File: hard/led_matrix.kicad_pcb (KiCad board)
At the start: 2 copper layers, 150 x 150 mm, 1038 parts, among them J1 MicroXNJ

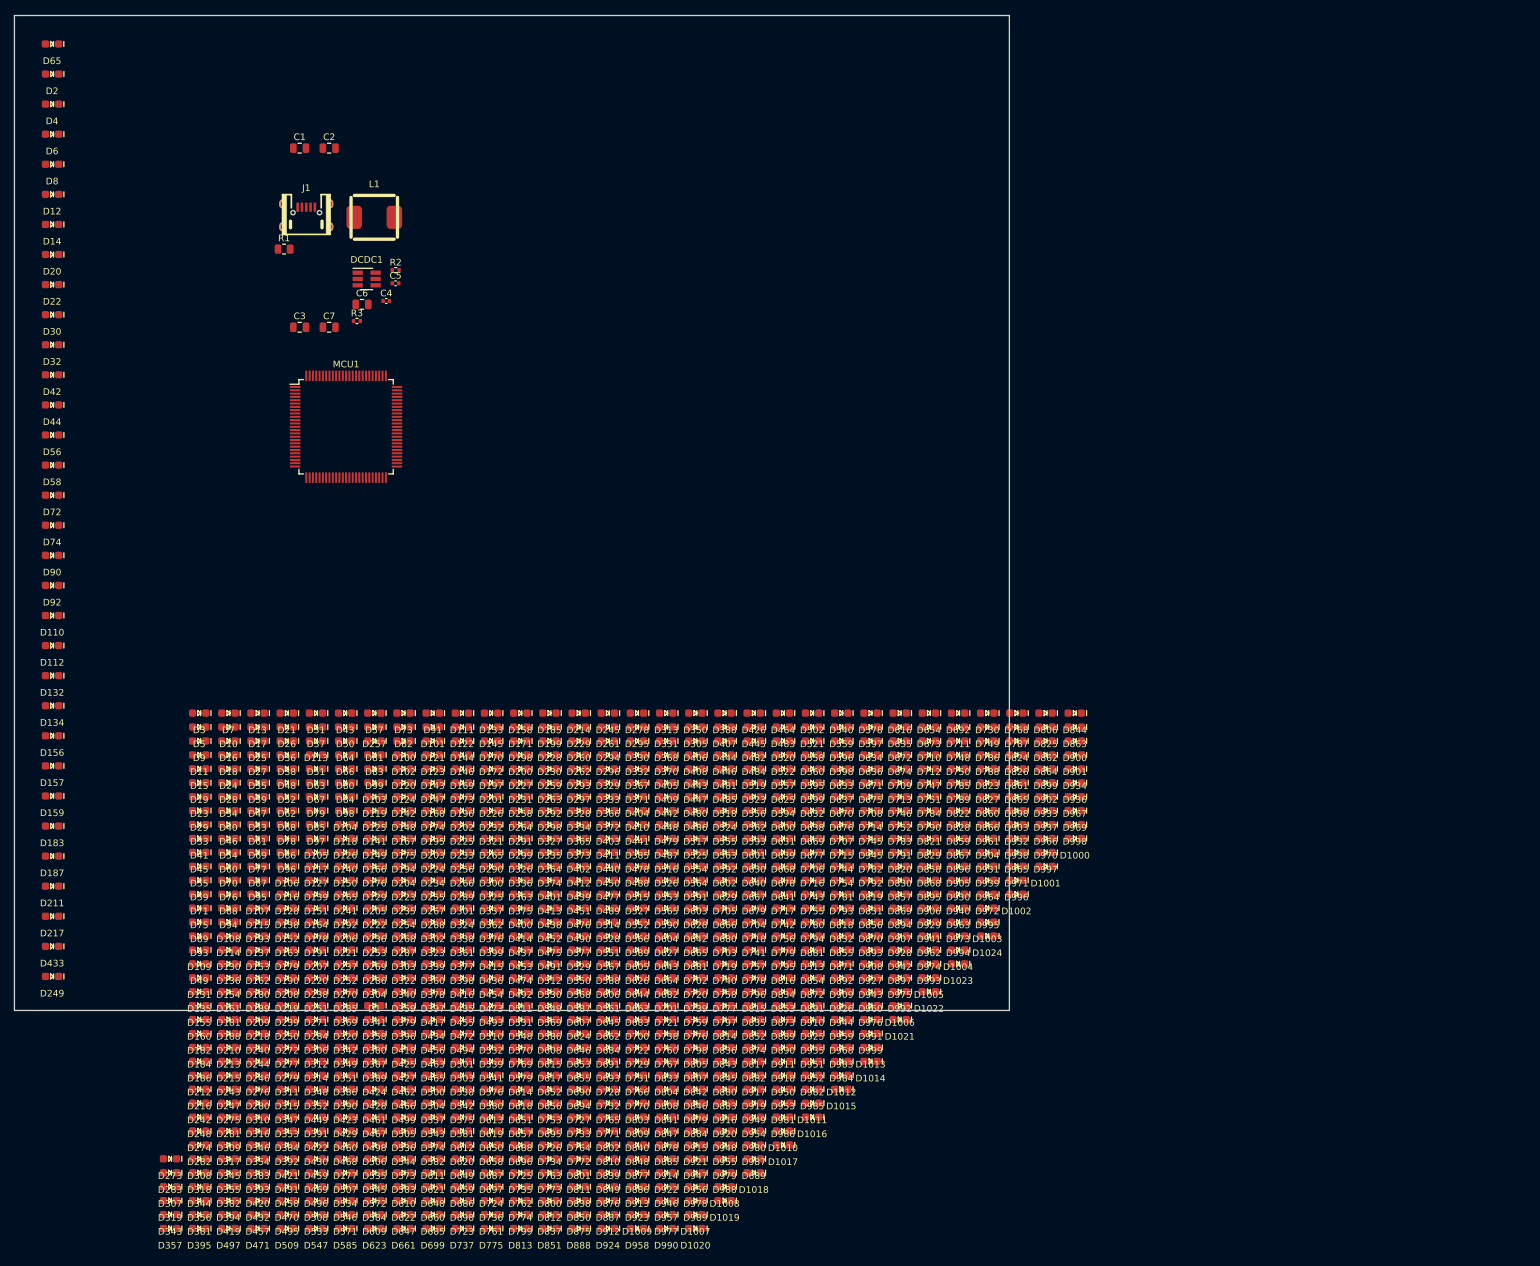
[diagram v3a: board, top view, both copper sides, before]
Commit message: 32x32 leds on board
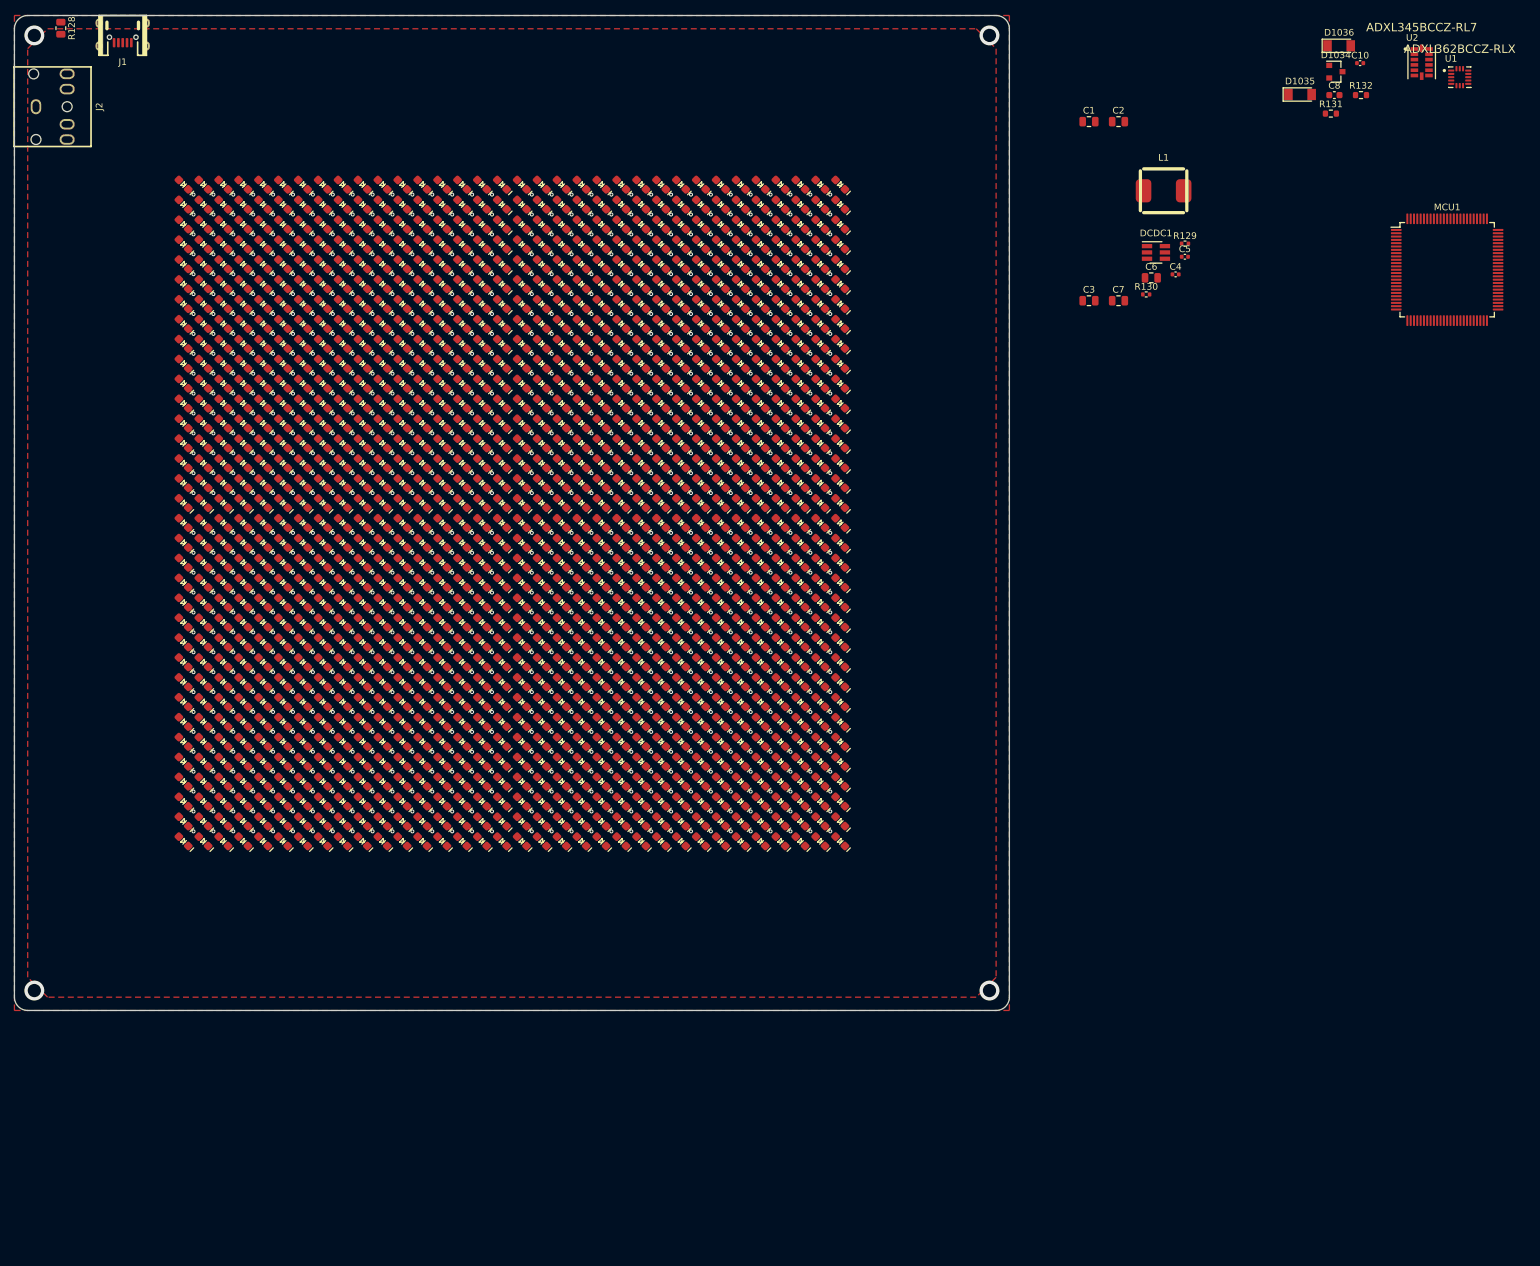
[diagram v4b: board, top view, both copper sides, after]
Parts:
- removed the D1 at (74.3, 177.2)
- removed D10, D100, D1000, D1001, D1002, D1003, D1004, D1005, D1006, D1007, D1008, D1009, D101, D1010, D1011, D1012, D1013, D1014, D1015, D1016, D1017, D1018, D1019, D102, D1020, D1021, D1022, D1023, D1024, D103, D104, D105, D106, D107, D108, D109, D11, D110, D111, D112, D113, D114, D115, D116, D117, D118, D119, D12, D120, D121, D122, D123, D124, D125, D126, D127, D128, D129, D13, D130, D131, D132, D133, D134, D135, D136, D137, D138, D139, D14, D140, D141, D142, D143, D144, D145, D146, D147, D148, D149, D15, D150, D151, D152, D153, D154, D155, D156, D157, D158, D159, D16, D160, D161, D162, D163, D164, D165, D166, D167, D168, D169, D17, D170, D171, D172, D173, D174, D175, D176, D177, D178, D179, D18, D180, D181, D182, D183, D184, D185, D186, D187, D188, D189, D19, D190, D191, D192, D193, D194, D195, D196, D197, D198, D199, D20, D200, D201, D202, D203, D204, D205, D206, D207, D208, D209, D21, D210, D211, D212, D213, D214, D215, D216, D217, D218, D219, D22, D220, D221, D222, D223, D224, D225, D226, D227, D228, D229, D23, D230, D231, D232, D233, D234, D235, D236, D237, D238, D239, D24, D240, D241, D242, D243, D244, D245, D246, D247, D248, D249, D25, D250, D251, D252, D253, D254, D255, D256, D257, D258, D259, D26, D260, D261, D262, D263, D264, D265, D266, D267, D268, D269, D27, D270, D271, D272, D273, D274, D275, D276, D277, D278, D279, D28, D280, D281, D282, D283, D284, D285, D286, D287, D288, D289, D29, D290, D291, D292, D293, D294, D295, D296, D297, D298, D299, D30, D300, D301, D302, D303, D304, D305, D306, D307, D308, D309, D31, D310, D311, D312, D313, D314, D315, D316, D317, D318, D319, D32, D320, D321, D322, D323, D324, D325, D326, D327, D328, D329, D330, D331, D332, D333, D334, D335, D336, D337, D338, D339, D340, D341, D342, D343, D344, D345, D346, D347, D348, D349, D350, D351, D352, D353, D354, D355, D356, D357, D358, D359, D36, D360, D361, D362, D363, D364, D365, D366, D367, D368, D369, D37, D370, D371, D372, D373, D374, D375, D376, D377, D378, D379, D38, D380, D381, D382, D383, D384, D385, D386, D387, D388, D389, D39, D390, D391, D392, D393, D394, D395, D396, D397, D398, D399, D4, D40, D400, D401, D402, D403, D404, D405, D406, D407, D408, D409, D41, D410, D411, D412, D413, D414, D415, D416, D417, D418, D419, D42, D420, D421, D422, D423, D424, D425, D426, D427, D428, D429, D43, D430, D431, D432, D433, D434, D435, D436, D437, D438, D439, D44, D440, D441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: LTST-S270TBKT, led_matrix:LED_LiteOn_LTST-S270TBKT
- removed the D2 at (25.7, 38.8)
- removed the D3 at (47.9, 135.2)
- removed the D33 at (47.9, 152.0)
- removed the D34 at (52.3, 147.8)
- removed the D35 at (56.7, 143.6)
- removed the D65 at (25.7, 34.3)
- removed the D66 at (69.9, 141.5)
- removed the D67 at (65.5, 145.7)
- removed R1: 0R1, Resistor_SMD:R_0805_2012Metric
- added C10: 0u1/6V3, Capacitor_SMD:C_0402_1005Metric, F.Cu at (222.9, 37.2)
- added C8: 1u/6V3, Capacitor_SMD:C_0603_1608Metric, F.Cu at (219.0, 42.0)
- added D1: LTST-S270TBKT, led_matrix:LED_LiteOn_LTST-S270TBKT, F.Cu at (54.5, 124.5)
- added D1: LTST-S270TBKT, led_matrix:LED_LiteOn_LTST-S270TBKT, F.Cu at (45.5, 151.5)
- added D1: LTST-S270TBKT, led_matrix:LED_LiteOn_LTST-S270TBKT, F.Cu at (132.5, 73.5)
- added D1: LTST-S270TBKT, led_matrix:LED_LiteOn_LTST-S270TBKT, F.Cu at (132.5, 55.5)
- added D1: LTST-S270TBKT, led_matrix:LED_LiteOn_LTST-S270TBKT, F.Cu at (141.5, 82.5)
- added D1: LTST-S270TBKT, led_matrix:LED_LiteOn_LTST-S270TBKT, F.Cu at (54.5, 91.5)
- added D1: LTST-S270TBKT, led_matrix:LED_LiteOn_LTST-S270TBKT, F.Cu at (45.5, 91.5)
- added D1: LTST-S270TBKT, led_matrix:LED_LiteOn_LTST-S270TBKT, F.Cu at (81.5, 91.5)
- added D1: LTST-S270TBKT, led_matrix:LED_LiteOn_LTST-S270TBKT, F.Cu at (45.5, 100.5)
- added D1: LTST-S270TBKT, led_matrix:LED_LiteOn_LTST-S270TBKT, F.Cu at (54.5, 100.5)
- added D1: LTST-S270TBKT, led_matrix:LED_LiteOn_LTST-S270TBKT, F.Cu at (45.5, 55.5)
- added D1: LTST-S270TBKT, led_matrix:LED_LiteOn_LTST-S270TBKT, F.Cu at (81.5, 55.5)
- added D1: LTST-S270TBKT, led_matrix:LED_LiteOn_LTST-S270TBKT, F.Cu at (54.5, 151.5)
- added D1: LTST-S270TBKT, led_matrix:LED_LiteOn_LTST-S270TBKT, F.Cu at (81.5, 73.5)
- added D1: LTST-S270TBKT, led_matrix:LED_LiteOn_LTST-S270TBKT, F.Cu at (81.5, 82.5)
- added D1: LTST-S270TBKT, led_matrix:LED_LiteOn_LTST-S270TBKT, F.Cu at (90.5, 82.5)
- added D1: LTST-S270TBKT, led_matrix:LED_LiteOn_LTST-S270TBKT, F.Cu at (90.5, 73.5)
- added D1: LTST-S270TBKT, led_matrix:LED_LiteOn_LTST-S270TBKT, F.Cu at (96.5, 106.5)
- added D1: LTST-S270TBKT, led_matrix:LED_LiteOn_LTST-S270TBKT, F.Cu at (105.5, 151.5)
- added D1: LTST-S270TBKT, led_matrix:LED_LiteOn_LTST-S270TBKT, F.Cu at (132.5, 133.5)
- added D1: LTST-S270TBKT, led_matrix:LED_LiteOn_LTST-S270TBKT, F.Cu at (132.5, 124.5)
- added D1: LTST-S270TBKT, led_matrix:LED_LiteOn_LTST-S270TBKT, F.Cu at (132.5, 106.5)
- added D1: LTST-S270TBKT, led_matrix:LED_LiteOn_LTST-S270TBKT, F.Cu at (141.5, 133.5)
- added D1: LTST-S270TBKT, led_matrix:LED_LiteOn_LTST-S270TBKT, F.Cu at (81.5, 142.5)
- added D1: LTST-S270TBKT, led_matrix:LED_LiteOn_LTST-S270TBKT, F.Cu at (54.5, 142.5)
- added D1: LTST-S270TBKT, led_matrix:LED_LiteOn_LTST-S270TBKT, F.Cu at (123.5, 142.5)
- added D1: LTST-S270TBKT, led_matrix:LED_LiteOn_LTST-S270TBKT, F.Cu at (132.5, 151.5)
- added D1: LTST-S270TBKT, led_matrix:LED_LiteOn_LTST-S270TBKT, F.Cu at (105.5, 115.5)
- added D1: LTST-S270TBKT, led_matrix:LED_LiteOn_LTST-S270TBKT, F.Cu at (96.5, 115.5)
- added D1: LTST-S270TBKT, led_matrix:LED_LiteOn_LTST-S270TBKT, F.Cu at (132.5, 142.5)
- added D1: LTST-S270TBKT, led_matrix:LED_LiteOn_LTST-S270TBKT, F.Cu at (96.5, 142.5)
- added D1: LTST-S270TBKT, led_matrix:LED_LiteOn_LTST-S270TBKT, F.Cu at (105.5, 142.5)
- added D1: LTST-S270TBKT, led_matrix:LED_LiteOn_LTST-S270TBKT, F.Cu at (105.5, 106.5)
- added D1: LTST-S270TBKT, led_matrix:LED_LiteOn_LTST-S270TBKT, F.Cu at (96.5, 151.5)
- added D1: LTST-S270TBKT, led_matrix:LED_LiteOn_LTST-S270TBKT, F.Cu at (81.5, 106.5)
- added D1: LTST-S270TBKT, led_matrix:LED_LiteOn_LTST-S270TBKT, F.Cu at (45.5, 73.5)
- added D1: LTST-S270TBKT, led_matrix:LED_LiteOn_LTST-S270TBKT, F.Cu at (63.5, 82.5)
- added D1: LTST-S270TBKT, led_matrix:LED_LiteOn_LTST-S270TBKT, F.Cu at (72.5, 82.5)
- added D1: LTST-S270TBKT, led_matrix:LED_LiteOn_LTST-S270TBKT, F.Cu at (45.5, 82.5)
- added D1: LTST-S270TBKT, led_matrix:LED_LiteOn_LTST-S270TBKT, F.Cu at (54.5, 82.5)
- added D1: LTST-S270TBKT, led_matrix:LED_LiteOn_LTST-S270TBKT, F.Cu at (54.5, 73.5)
- added D1: LTST-S270TBKT, led_matrix:LED_LiteOn_LTST-S270TBKT, F.Cu at (72.5, 73.5)
- added D1: LTST-S270TBKT, led_matrix:LED_LiteOn_LTST-S270TBKT, F.Cu at (63.5, 73.5)
- added D1: LTST-S270TBKT, led_matrix:LED_LiteOn_LTST-S270TBKT, F.Cu at (90.5, 55.5)
- added D1: LTST-S270TBKT, led_matrix:LED_LiteOn_LTST-S270TBKT, F.Cu at (90.5, 64.5)
- added D1: LTST-S270TBKT, led_matrix:LED_LiteOn_LTST-S270TBKT, F.Cu at (81.5, 124.5)
- added D1: LTST-S270TBKT, led_matrix:LED_LiteOn_LTST-S270TBKT, F.Cu at (81.5, 64.5)
- added D1: LTST-S270TBKT, led_matrix:LED_LiteOn_LTST-S270TBKT, F.Cu at (63.5, 64.5)
- added D1: LTST-S270TBKT, led_matrix:LED_LiteOn_LTST-S270TBKT, F.Cu at (72.5, 64.5)
- added D1: LTST-S270TBKT, led_matrix:LED_LiteOn_LTST-S270TBKT, F.Cu at (72.5, 55.5)
- added D1: LTST-S270TBKT, led_matrix:LED_LiteOn_LTST-S270TBKT, F.Cu at (63.5, 55.5)
- added D1: LTST-S270TBKT, led_matrix:LED_LiteOn_LTST-S270TBKT, F.Cu at (81.5, 133.5)
- added D1: LTST-S270TBKT, led_matrix:LED_LiteOn_LTST-S270TBKT, F.Cu at (90.5, 133.5)
- added D1: LTST-S270TBKT, led_matrix:LED_LiteOn_LTST-S270TBKT, F.Cu at (63.5, 133.5)
- added D1: LTST-S270TBKT, led_matrix:LED_LiteOn_LTST-S270TBKT, F.Cu at (90.5, 124.5)
- added D1: LTST-S270TBKT, led_matrix:LED_LiteOn_LTST-S270TBKT, F.Cu at (45.5, 124.5)
- added D1: LTST-S270TBKT, led_matrix:LED_LiteOn_LTST-S270TBKT, F.Cu at (54.5, 133.5)
- added D1: LTST-S270TBKT, led_matrix:LED_LiteOn_LTST-S270TBKT, F.Cu at (90.5, 91.5)
- added D1: LTST-S270TBKT, led_matrix:LED_LiteOn_LTST-S270TBKT, F.Cu at (90.5, 100.5)
- added D1: LTST-S270TBKT, led_matrix:LED_LiteOn_LTST-S270TBKT, F.Cu at (63.5, 100.5)
- added D1: LTST-S270TBKT, led_matrix:LED_LiteOn_LTST-S270TBKT, F.Cu at (72.5, 100.5)
- added D1: LTST-S270TBKT, led_matrix:LED_LiteOn_LTST-S270TBKT, F.Cu at (81.5, 100.5)
- added D1: LTST-S270TBKT, led_matrix:LED_LiteOn_LTST-S270TBKT, F.Cu at (72.5, 91.5)
- added D1: LTST-S270TBKT, led_matrix:LED_LiteOn_LTST-S270TBKT, F.Cu at (63.5, 91.5)
- added D1: LTST-S270TBKT, led_matrix:LED_LiteOn_LTST-S270TBKT, F.Cu at (45.5, 64.5)
- added D1: LTST-S270TBKT, led_matrix:LED_LiteOn_LTST-S270TBKT, F.Cu at (54.5, 64.5)
- added D1: LTST-S270TBKT, led_matrix:LED_LiteOn_LTST-S270TBKT, F.Cu at (90.5, 142.5)
- added D1: LTST-S270TBKT, led_matrix:LED_LiteOn_LTST-S270TBKT, F.Cu at (72.5, 133.5)
- added D1: LTST-S270TBKT, led_matrix:LED_LiteOn_LTST-S270TBKT, F.Cu at (63.5, 151.5)
- added D1: LTST-S270TBKT, led_matrix:LED_LiteOn_LTST-S270TBKT, F.Cu at (90.5, 151.5)
- added D1: LTST-S270TBKT, led_matrix:LED_LiteOn_LTST-S270TBKT, F.Cu at (72.5, 151.5)
- added D1: LTST-S270TBKT, led_matrix:LED_LiteOn_LTST-S270TBKT, F.Cu at (81.5, 151.5)
- added D1: LTST-S270TBKT, led_matrix:LED_LiteOn_LTST-S270TBKT, F.Cu at (72.5, 142.5)
- added D1: LTST-S270TBKT, led_matrix:LED_LiteOn_LTST-S270TBKT, F.Cu at (63.5, 142.5)
- added D1: LTST-S270TBKT, led_matrix:LED_LiteOn_LTST-S270TBKT, F.Cu at (45.5, 115.5)
- added D1: LTST-S270TBKT, led_matrix:LED_LiteOn_LTST-S270TBKT, F.Cu at (54.5, 115.5)
- added D1: LTST-S270TBKT, led_matrix:LED_LiteOn_LTST-S270TBKT, F.Cu at (54.5, 106.5)
- added D1: LTST-S270TBKT, led_matrix:LED_LiteOn_LTST-S270TBKT, F.Cu at (123.5, 133.5)
- added D1: LTST-S270TBKT, led_matrix:LED_LiteOn_LTST-S270TBKT, F.Cu at (45.5, 133.5)
- added D1: LTST-S270TBKT, led_matrix:LED_LiteOn_LTST-S270TBKT, F.Cu at (105.5, 133.5)
- added D1: LTST-S270TBKT, led_matrix:LED_LiteOn_LTST-S270TBKT, F.Cu at (54.5, 55.5)
- added D1: LTST-S270TBKT, led_matrix:LED_LiteOn_LTST-S270TBKT, F.Cu at (123.5, 82.5)
- added D1: LTST-S270TBKT, led_matrix:LED_LiteOn_LTST-S270TBKT, F.Cu at (105.5, 82.5)
- added D1: LTST-S270TBKT, led_matrix:LED_LiteOn_LTST-S270TBKT, F.Cu at (114.5, 82.5)
- added D1: LTST-S270TBKT, led_matrix:LED_LiteOn_LTST-S270TBKT, F.Cu at (96.5, 82.5)
- added D1: LTST-S270TBKT, led_matrix:LED_LiteOn_LTST-S270TBKT, F.Cu at (96.5, 73.5)
- added D1: LTST-S270TBKT, led_matrix:LED_LiteOn_LTST-S270TBKT, F.Cu at (141.5, 73.5)
- added D1: LTST-S270TBKT, led_matrix:LED_LiteOn_LTST-S270TBKT, F.Cu at (105.5, 73.5)
- added D1: LTST-S270TBKT, led_matrix:LED_LiteOn_LTST-S270TBKT, F.Cu at (123.5, 73.5)
- added D1: LTST-S270TBKT, led_matrix:LED_LiteOn_LTST-S270TBKT, F.Cu at (72.5, 124.5)
- added D1: LTST-S270TBKT, led_matrix:LED_LiteOn_LTST-S270TBKT, F.Cu at (141.5, 64.5)
- added D1: LTST-S270TBKT, led_matrix:LED_LiteOn_LTST-S270TBKT, F.Cu at (141.5, 55.5)
- added D1: LTST-S270TBKT, led_matrix:LED_LiteOn_LTST-S270TBKT, F.Cu at (114.5, 73.5)
- added D1: LTST-S270TBKT, led_matrix:LED_LiteOn_LTST-S270TBKT, F.Cu at (132.5, 64.5)
- added D1: LTST-S270TBKT, led_matrix:LED_LiteOn_LTST-S270TBKT, F.Cu at (123.5, 64.5)
- added D1: LTST-S270TBKT, led_matrix:LED_LiteOn_LTST-S270TBKT, F.Cu at (114.5, 64.5)
- added D1: LTST-S270TBKT, led_matrix:LED_LiteOn_LTST-S270TBKT, F.Cu at (123.5, 55.5)
- added D1: LTST-S270TBKT, led_matrix:LED_LiteOn_LTST-S270TBKT, F.Cu at (114.5, 55.5)
- added D1: LTST-S270TBKT, led_matrix:LED_LiteOn_LTST-S270TBKT, F.Cu at (72.5, 115.5)
- added D1: LTST-S270TBKT, led_matrix:LED_LiteOn_LTST-S270TBKT, F.Cu at (90.5, 115.5)
- added D1: LTST-S270TBKT, led_matrix:LED_LiteOn_LTST-S270TBKT, F.Cu at (63.5, 124.5)
- added D1: LTST-S270TBKT, led_matrix:LED_LiteOn_LTST-S270TBKT, F.Cu at (63.5, 115.5)
- added D1: LTST-S270TBKT, led_matrix:LED_LiteOn_LTST-S270TBKT, F.Cu at (72.5, 106.5)
- added D1: LTST-S270TBKT, led_matrix:LED_LiteOn_LTST-S270TBKT, F.Cu at (81.5, 115.5)
- added D1: LTST-S270TBKT, led_matrix:LED_LiteOn_LTST-S270TBKT, F.Cu at (63.5, 106.5)
- added D1: LTST-S270TBKT, led_matrix:LED_LiteOn_LTST-S270TBKT, F.Cu at (114.5, 133.5)
- added D1: LTST-S270TBKT, led_matrix:LED_LiteOn_LTST-S270TBKT, F.Cu at (141.5, 124.5)
- added D1: LTST-S270TBKT, led_matrix:LED_LiteOn_LTST-S270TBKT, F.Cu at (96.5, 133.5)
- added D1: LTST-S270TBKT, led_matrix:LED_LiteOn_LTST-S270TBKT, F.Cu at (96.5, 124.5)
- added D1: LTST-S270TBKT, led_matrix:LED_LiteOn_LTST-S270TBKT, F.Cu at (123.5, 124.5)
- added D1: LTST-S270TBKT, led_matrix:LED_LiteOn_LTST-S270TBKT, F.Cu at (105.5, 124.5)
- added D1: LTST-S270TBKT, led_matrix:LED_LiteOn_LTST-S270TBKT, F.Cu at (90.5, 106.5)
- added D1: LTST-S270TBKT, led_matrix:LED_LiteOn_LTST-S270TBKT, F.Cu at (141.5, 115.5)
- added D1: LTST-S270TBKT, led_matrix:LED_LiteOn_LTST-S270TBKT, F.Cu at (123.5, 115.5)
- added D1: LTST-S270TBKT, led_matrix:LED_LiteOn_LTST-S270TBKT, F.Cu at (114.5, 106.5)
- added D1: LTST-S270TBKT, led_matrix:LED_LiteOn_LTST-S270TBKT, F.Cu at (114.5, 124.5)
- added D1: LTST-S270TBKT, led_matrix:LED_LiteOn_LTST-S270TBKT, F.Cu at (141.5, 106.5)
- added D1: LTST-S270TBKT, led_matrix:LED_LiteOn_LTST-S270TBKT, F.Cu at (132.5, 115.5)
- added D1: LTST-S270TBKT, led_matrix:LED_LiteOn_LTST-S270TBKT, F.Cu at (114.5, 115.5)
- added D1: LTST-S270TBKT, led_matrix:LED_LiteOn_LTST-S270TBKT, F.Cu at (123.5, 106.5)
- added D1: LTST-S270TBKT, led_matrix:LED_LiteOn_LTST-S270TBKT, F.Cu at (141.5, 142.5)
- added D1: LTST-S270TBKT, led_matrix:LED_LiteOn_LTST-S270TBKT, F.Cu at (123.5, 151.5)
- added D1: LTST-S270TBKT, led_matrix:LED_LiteOn_LTST-S270TBKT, F.Cu at (45.5, 142.5)
- added D1: LTST-S270TBKT, led_matrix:LED_LiteOn_LTST-S270TBKT, F.Cu at (141.5, 151.5)
- added D1: LTST-S270TBKT, led_matrix:LED_LiteOn_LTST-S270TBKT, F.Cu at (114.5, 142.5)
- added D1: LTST-S270TBKT, led_matrix:LED_LiteOn_LTST-S270TBKT, F.Cu at (114.5, 151.5)
- added D1: LTST-S270TBKT, led_matrix:LED_LiteOn_LTST-S270TBKT, F.Cu at (114.5, 100.5)
- added D1: LTST-S270TBKT, led_matrix:LED_LiteOn_LTST-S270TBKT, F.Cu at (141.5, 100.5)
- added D1: LTST-S270TBKT, led_matrix:LED_LiteOn_LTST-S270TBKT, F.Cu at (114.5, 91.5)
- added D1: LTST-S270TBKT, led_matrix:LED_LiteOn_LTST-S270TBKT, F.Cu at (141.5, 91.5)
- added D1: LTST-S270TBKT, led_matrix:LED_LiteOn_LTST-S270TBKT, F.Cu at (123.5, 100.5)
- added D1: LTST-S270TBKT, led_matrix:LED_LiteOn_LTST-S270TBKT, F.Cu at (123.5, 91.5)
- added D1: LTST-S270TBKT, led_matrix:LED_LiteOn_LTST-S270TBKT, F.Cu at (132.5, 100.5)
- added D1: LTST-S270TBKT, led_matrix:LED_LiteOn_LTST-S270TBKT, F.Cu at (45.5, 106.5)
- added D1: LTST-S270TBKT, led_matrix:LED_LiteOn_LTST-S270TBKT, F.Cu at (96.5, 64.5)
- added D1: LTST-S270TBKT, led_matrix:LED_LiteOn_LTST-S270TBKT, F.Cu at (105.5, 64.5)
- added D1: LTST-S270TBKT, led_matrix:LED_LiteOn_LTST-S270TBKT, F.Cu at (132.5, 91.5)
- added D1: LTST-S270TBKT, led_matrix:LED_LiteOn_LTST-S270TBKT, F.Cu at (105.5, 91.5)
- added D1: LTST-S270TBKT, led_matrix:LED_LiteOn_LTST-S270TBKT, F.Cu at (96.5, 91.5)
- added D1: LTST-S270TBKT, led_matrix:LED_LiteOn_LTST-S270TBKT, F.Cu at (96.5, 100.5)
- added D1: LTST-S270TBKT, led_matrix:LED_LiteOn_LTST-S270TBKT, F.Cu at (105.5, 55.5)
- added D1: LTST-S270TBKT, led_matrix:LED_LiteOn_LTST-S270TBKT, F.Cu at (105.5, 100.5)
- added D1: LTST-S270TBKT, led_matrix:LED_LiteOn_LTST-S270TBKT, F.Cu at (96.5, 55.5)
- added D1: LTST-S270TBKT, led_matrix:LED_LiteOn_LTST-S270TBKT, F.Cu at (132.5, 82.5)
- added D1034: PSM712-LF-T7, Package_TO_SOT_SMD:SOT-23, F.Cu at (219.2, 38.5)
- added D1035: D_Zener, Diode_SMD:D_MiniMELF, F.Cu at (213.8, 41.9)
- added D1036: D_Zener, Diode_SMD:D_MiniMELF, F.Cu at (219.7, 34.6)
- added D2: LTST-S270TBKT, led_matrix:LED_LiteOn_LTST-S270TBKT, F.Cu at (54.5, 127.5)
- added D2: LTST-S270TBKT, led_matrix:LED_LiteOn_LTST-S270TBKT, F.Cu at (54.5, 154.5)
- added D2: LTST-S270TBKT, led_matrix:LED_LiteOn_LTST-S270TBKT, F.Cu at (90.5, 58.5)
- added D2: LTST-S270TBKT, led_matrix:LED_LiteOn_LTST-S270TBKT, F.Cu at (54.5, 94.5)
- added D2: LTST-S270TBKT, led_matrix:LED_LiteOn_LTST-S270TBKT, F.Cu at (90.5, 94.5)
- added D2: LTST-S270TBKT, led_matrix:LED_LiteOn_LTST-S270TBKT, F.Cu at (45.5, 94.5)
- added D2: LTST-S270TBKT, led_matrix:LED_LiteOn_LTST-S270TBKT, F.Cu at (81.5, 94.5)
- added D2: LTST-S270TBKT, led_matrix:LED_LiteOn_LTST-S270TBKT, F.Cu at (45.5, 103.5)
- added D2: LTST-S270TBKT, led_matrix:LED_LiteOn_LTST-S270TBKT, F.Cu at (54.5, 103.5)
- added D2: LTST-S270TBKT, led_matrix:LED_LiteOn_LTST-S270TBKT, F.Cu at (45.5, 58.5)
- added D2: LTST-S270TBKT, led_matrix:LED_LiteOn_LTST-S270TBKT, F.Cu at (90.5, 85.5)
- added D2: LTST-S270TBKT, led_matrix:LED_LiteOn_LTST-S270TBKT, F.Cu at (81.5, 58.5)
- added D2: LTST-S270TBKT, led_matrix:LED_LiteOn_LTST-S270TBKT, F.Cu at (81.5, 145.5)
- added D2: LTST-S270TBKT, led_matrix:LED_LiteOn_LTST-S270TBKT, F.Cu at (81.5, 85.5)
- added D2: LTST-S270TBKT, led_matrix:LED_LiteOn_LTST-S270TBKT, F.Cu at (90.5, 76.5)
- added D2: LTST-S270TBKT, led_matrix:LED_LiteOn_LTST-S270TBKT, F.Cu at (81.5, 76.5)
- added D2: LTST-S270TBKT, led_matrix:LED_LiteOn_LTST-S270TBKT, F.Cu at (96.5, 154.5)
- added D2: LTST-S270TBKT, led_matrix:LED_LiteOn_LTST-S270TBKT, F.Cu at (96.5, 109.5)
- added D2: LTST-S270TBKT, led_matrix:LED_LiteOn_LTST-S270TBKT, F.Cu at (105.5, 154.5)
- added D2: LTST-S270TBKT, led_matrix:LED_LiteOn_LTST-S270TBKT, F.Cu at (141.5, 136.5)
- added D2: LTST-S270TBKT, led_matrix:LED_LiteOn_LTST-S270TBKT, F.Cu at (132.5, 109.5)
- added D2: LTST-S270TBKT, led_matrix:LED_LiteOn_LTST-S270TBKT, F.Cu at (90.5, 109.5)
- added D2: LTST-S270TBKT, led_matrix:LED_LiteOn_LTST-S270TBKT, F.Cu at (54.5, 145.5)
- added D2: LTST-S270TBKT, led_matrix:LED_LiteOn_LTST-S270TBKT, F.Cu at (45.5, 154.5)
- added D2: LTST-S270TBKT, led_matrix:LED_LiteOn_LTST-S270TBKT, F.Cu at (45.5, 145.5)
- added D2: LTST-S270TBKT, led_matrix:LED_LiteOn_LTST-S270TBKT, F.Cu at (90.5, 145.5)
- added D2: LTST-S270TBKT, led_matrix:LED_LiteOn_LTST-S270TBKT, F.Cu at (123.5, 145.5)
- added D2: LTST-S270TBKT, led_matrix:LED_LiteOn_LTST-S270TBKT, F.Cu at (141.5, 145.5)
- added D2: LTST-S270TBKT, led_matrix:LED_LiteOn_LTST-S270TBKT, F.Cu at (105.5, 118.5)
- added D2: LTST-S270TBKT, led_matrix:LED_LiteOn_LTST-S270TBKT, F.Cu at (96.5, 118.5)
- added D2: LTST-S270TBKT, led_matrix:LED_LiteOn_LTST-S270TBKT, F.Cu at (105.5, 145.5)
- added D2: LTST-S270TBKT, led_matrix:LED_LiteOn_LTST-S270TBKT, F.Cu at (96.5, 145.5)
- added D2: LTST-S270TBKT, led_matrix:LED_LiteOn_LTST-S270TBKT, F.Cu at (141.5, 109.5)
- added D2: LTST-S270TBKT, led_matrix:LED_LiteOn_LTST-S270TBKT, F.Cu at (132.5, 145.5)
- added D2: LTST-S270TBKT, led_matrix:LED_LiteOn_LTST-S270TBKT, F.Cu at (90.5, 136.5)
- added D2: LTST-S270TBKT, led_matrix:LED_LiteOn_LTST-S270TBKT, F.Cu at (105.5, 109.5)
- added D2: LTST-S270TBKT, led_matrix:LED_LiteOn_LTST-S270TBKT, F.Cu at (54.5, 85.5)
- added D2: LTST-S270TBKT, led_matrix:LED_LiteOn_LTST-S270TBKT, F.Cu at (45.5, 85.5)
- added D2: LTST-S270TBKT, led_matrix:LED_LiteOn_LTST-S270TBKT, F.Cu at (54.5, 76.5)
- added D2: LTST-S270TBKT, led_matrix:LED_LiteOn_LTST-S270TBKT, F.Cu at (45.5, 76.5)
- added D2: LTST-S270TBKT, led_matrix:LED_LiteOn_LTST-S270TBKT, F.Cu at (72.5, 76.5)
- added D2: LTST-S270TBKT, led_matrix:LED_LiteOn_LTST-S270TBKT, F.Cu at (72.5, 85.5)
- added D2: LTST-S270TBKT, led_matrix:LED_LiteOn_LTST-S270TBKT, F.Cu at (63.5, 85.5)
- added D2: LTST-S270TBKT, led_matrix:LED_LiteOn_LTST-S270TBKT, F.Cu at (63.5, 76.5)
- added D2: LTST-S270TBKT, led_matrix:LED_LiteOn_LTST-S270TBKT, F.Cu at (90.5, 67.5)
- added D2: LTST-S270TBKT, led_matrix:LED_LiteOn_LTST-S270TBKT, F.Cu at (81.5, 136.5)
- added D2: LTST-S270TBKT, led_matrix:LED_LiteOn_LTST-S270TBKT, F.Cu at (81.5, 67.5)
- added D2: LTST-S270TBKT, led_matrix:LED_LiteOn_LTST-S270TBKT, F.Cu at (72.5, 58.5)
- added D2: LTST-S270TBKT, led_matrix:LED_LiteOn_LTST-S270TBKT, F.Cu at (72.5, 67.5)
- added D2: LTST-S270TBKT, led_matrix:LED_LiteOn_LTST-S270TBKT, F.Cu at (63.5, 67.5)
- added D2: LTST-S270TBKT, led_matrix:LED_LiteOn_LTST-S270TBKT, F.Cu at (63.5, 58.5)
- added D2: LTST-S270TBKT, led_matrix:LED_LiteOn_LTST-S270TBKT, F.Cu at (81.5, 109.5)
- added D2: LTST-S270TBKT, led_matrix:LED_LiteOn_LTST-S270TBKT, F.Cu at (90.5, 127.5)
- added D2: LTST-S270TBKT, led_matrix:LED_LiteOn_LTST-S270TBKT, F.Cu at (81.5, 127.5)
- added D2: LTST-S270TBKT, led_matrix:LED_LiteOn_LTST-S270TBKT, F.Cu at (81.5, 103.5)
- added D2: LTST-S270TBKT, led_matrix:LED_LiteOn_LTST-S270TBKT, F.Cu at (90.5, 103.5)
- added D2: LTST-S270TBKT, led_matrix:LED_LiteOn_LTST-S270TBKT, F.Cu at (45.5, 127.5)
- added D2: LTST-S270TBKT, led_matrix:LED_LiteOn_LTST-S270TBKT, F.Cu at (72.5, 94.5)
- added D2: LTST-S270TBKT, led_matrix:LED_LiteOn_LTST-S270TBKT, F.Cu at (63.5, 103.5)
- added D2: LTST-S270TBKT, led_matrix:LED_LiteOn_LTST-S270TBKT, F.Cu at (72.5, 103.5)
- added D2: LTST-S270TBKT, led_matrix:LED_LiteOn_LTST-S270TBKT, F.Cu at (63.5, 94.5)
- added D2: LTST-S270TBKT, led_matrix:LED_LiteOn_LTST-S270TBKT, F.Cu at (54.5, 67.5)
- added D2: LTST-S270TBKT, led_matrix:LED_LiteOn_LTST-S270TBKT, F.Cu at (45.5, 67.5)
- added D2: LTST-S270TBKT, led_matrix:LED_LiteOn_LTST-S270TBKT, F.Cu at (81.5, 154.5)
- added D2: LTST-S270TBKT, led_matrix:LED_LiteOn_LTST-S270TBKT, F.Cu at (90.5, 154.5)
- added D2: LTST-S270TBKT, led_matrix:LED_LiteOn_LTST-S270TBKT, F.Cu at (72.5, 145.5)
- added D2: LTST-S270TBKT, led_matrix:LED_LiteOn_LTST-S270TBKT, F.Cu at (63.5, 145.5)
- added D2: LTST-S270TBKT, led_matrix:LED_LiteOn_LTST-S270TBKT, F.Cu at (45.5, 136.5)
- added D2: LTST-S270TBKT, led_matrix:LED_LiteOn_LTST-S270TBKT, F.Cu at (54.5, 109.5)
- added D2: LTST-S270TBKT, led_matrix:LED_LiteOn_LTST-S270TBKT, F.Cu at (54.5, 118.5)
- added D2: LTST-S270TBKT, led_matrix:LED_LiteOn_LTST-S270TBKT, F.Cu at (72.5, 154.5)
- added D2: LTST-S270TBKT, led_matrix:LED_LiteOn_LTST-S270TBKT, F.Cu at (63.5, 154.5)
- added D2: LTST-S270TBKT, led_matrix:LED_LiteOn_LTST-S270TBKT, F.Cu at (45.5, 118.5)
- added D2: LTST-S270TBKT, led_matrix:LED_LiteOn_LTST-S270TBKT, F.Cu at (96.5, 136.5)
- added D2: LTST-S270TBKT, led_matrix:LED_LiteOn_LTST-S270TBKT, F.Cu at (132.5, 127.5)
- added D2: LTST-S270TBKT, led_matrix:LED_LiteOn_LTST-S270TBKT, F.Cu at (132.5, 136.5)
- added D2: LTST-S270TBKT, led_matrix:LED_LiteOn_LTST-S270TBKT, F.Cu at (54.5, 58.5)
- added D2: LTST-S270TBKT, led_matrix:LED_LiteOn_LTST-S270TBKT, F.Cu at (96.5, 85.5)
- added D2: LTST-S270TBKT, led_matrix:LED_LiteOn_LTST-S270TBKT, F.Cu at (54.5, 136.5)
- added D2: LTST-S270TBKT, led_matrix:LED_LiteOn_LTST-S270TBKT, F.Cu at (132.5, 76.5)
- added D2: LTST-S270TBKT, led_matrix:LED_LiteOn_LTST-S270TBKT, F.Cu at (132.5, 85.5)
- added D2: LTST-S270TBKT, led_matrix:LED_LiteOn_LTST-S270TBKT, F.Cu at (141.5, 76.5)
- added D2: LTST-S270TBKT, led_matrix:LED_LiteOn_LTST-S270TBKT, F.Cu at (105.5, 85.5)
- added D2: LTST-S270TBKT, led_matrix:LED_LiteOn_LTST-S270TBKT, F.Cu at (105.5, 76.5)
- added D2: LTST-S270TBKT, led_matrix:LED_LiteOn_LTST-S270TBKT, F.Cu at (123.5, 76.5)
- added D2: LTST-S270TBKT, led_matrix:LED_LiteOn_LTST-S270TBKT, F.Cu at (96.5, 76.5)
- added D2: LTST-S270TBKT, led_matrix:LED_LiteOn_LTST-S270TBKT, F.Cu at (114.5, 85.5)
- added D2: LTST-S270TBKT, led_matrix:LED_LiteOn_LTST-S270TBKT, F.Cu at (141.5, 67.5)
- added D2: LTST-S270TBKT, led_matrix:LED_LiteOn_LTST-S270TBKT, F.Cu at (114.5, 76.5)
- added D2: LTST-S270TBKT, led_matrix:LED_LiteOn_LTST-S270TBKT, F.Cu at (72.5, 127.5)
- added D2: LTST-S270TBKT, led_matrix:LED_LiteOn_LTST-S270TBKT, F.Cu at (123.5, 85.5)
- added D2: LTST-S270TBKT, led_matrix:LED_LiteOn_LTST-S270TBKT, F.Cu at (132.5, 67.5)
- added D2: LTST-S270TBKT, led_matrix:LED_LiteOn_LTST-S270TBKT, F.Cu at (123.5, 58.5)
- added D2: LTST-S270TBKT, led_matrix:LED_LiteOn_LTST-S270TBKT, F.Cu at (114.5, 67.5)
- added D2: LTST-S270TBKT, led_matrix:LED_LiteOn_LTST-S270TBKT, F.Cu at (114.5, 58.5)
- added D2: LTST-S270TBKT, led_matrix:LED_LiteOn_LTST-S270TBKT, F.Cu at (123.5, 67.5)
- added D2: LTST-S270TBKT, led_matrix:LED_LiteOn_LTST-S270TBKT, F.Cu at (81.5, 118.5)
- added D2: LTST-S270TBKT, led_matrix:LED_LiteOn_LTST-S270TBKT, F.Cu at (63.5, 109.5)
- added D2: LTST-S270TBKT, led_matrix:LED_LiteOn_LTST-S270TBKT, F.Cu at (90.5, 118.5)
- added D2: LTST-S270TBKT, led_matrix:LED_LiteOn_LTST-S270TBKT, F.Cu at (72.5, 109.5)
- added D2: LTST-S270TBKT, led_matrix:LED_LiteOn_LTST-S270TBKT, F.Cu at (63.5, 136.5)
- added D2: LTST-S270TBKT, led_matrix:LED_LiteOn_LTST-S270TBKT, F.Cu at (72.5, 118.5)
- added D2: LTST-S270TBKT, led_matrix:LED_LiteOn_LTST-S270TBKT, F.Cu at (63.5, 118.5)
- added D2: LTST-S270TBKT, led_matrix:LED_LiteOn_LTST-S270TBKT, F.Cu at (123.5, 127.5)
- added D2: LTST-S270TBKT, led_matrix:LED_LiteOn_LTST-S270TBKT, F.Cu at (105.5, 127.5)
- added D2: LTST-S270TBKT, led_matrix:LED_LiteOn_LTST-S270TBKT, F.Cu at (141.5, 127.5)
- added D2: LTST-S270TBKT, led_matrix:LED_LiteOn_LTST-S270TBKT, F.Cu at (105.5, 136.5)
- added D2: LTST-S270TBKT, led_matrix:LED_LiteOn_LTST-S270TBKT, F.Cu at (96.5, 127.5)
- added D2: LTST-S270TBKT, led_matrix:LED_LiteOn_LTST-S270TBKT, F.Cu at (114.5, 136.5)
- added D2: LTST-S270TBKT, led_matrix:LED_LiteOn_LTST-S270TBKT, F.Cu at (141.5, 118.5)
- added D2: LTST-S270TBKT, led_matrix:LED_LiteOn_LTST-S270TBKT, F.Cu at (114.5, 127.5)
- added D2: LTST-S270TBKT, led_matrix:LED_LiteOn_LTST-S270TBKT, F.Cu at (72.5, 136.5)
- added D2: LTST-S270TBKT, led_matrix:LED_LiteOn_LTST-S270TBKT, F.Cu at (123.5, 136.5)
- added D2: LTST-S270TBKT, led_matrix:LED_LiteOn_LTST-S270TBKT, F.Cu at (123.5, 109.5)
- added D2: LTST-S270TBKT, led_matrix:LED_LiteOn_LTST-S270TBKT, F.Cu at (132.5, 118.5)
- added D2: LTST-S270TBKT, led_matrix:LED_LiteOn_LTST-S270TBKT, F.Cu at (114.5, 118.5)
- added D2: LTST-S270TBKT, led_matrix:LED_LiteOn_LTST-S270TBKT, F.Cu at (114.5, 109.5)
- added D2: LTST-S270TBKT, led_matrix:LED_LiteOn_LTST-S270TBKT, F.Cu at (123.5, 118.5)
- added D2: LTST-S270TBKT, led_matrix:LED_LiteOn_LTST-S270TBKT, F.Cu at (114.5, 145.5)
- added D2: LTST-S270TBKT, led_matrix:LED_LiteOn_LTST-S270TBKT, F.Cu at (132.5, 154.5)
- added D2: LTST-S270TBKT, led_matrix:LED_LiteOn_LTST-S270TBKT, F.Cu at (114.5, 154.5)
- added D2: LTST-S270TBKT, led_matrix:LED_LiteOn_LTST-S270TBKT, F.Cu at (141.5, 154.5)
- added D2: LTST-S270TBKT, led_matrix:LED_LiteOn_LTST-S270TBKT, F.Cu at (63.5, 127.5)
- added D2: LTST-S270TBKT, led_matrix:LED_LiteOn_LTST-S270TBKT, F.Cu at (123.5, 154.5)
- added D2: LTST-S270TBKT, led_matrix:LED_LiteOn_LTST-S270TBKT, F.Cu at (132.5, 103.5)
- added D2: LTST-S270TBKT, led_matrix:LED_LiteOn_LTST-S270TBKT, F.Cu at (123.5, 103.5)
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- renumbered R2 to R129, R3 to R130
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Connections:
- DCDC1 pad 5: Net-(DCDC1-Pad5) -> (no net)
- J1 pad 2: Net-(J1-Pad2) -> (no net)
- J1 pad 3: Net-(J1-Pad3) -> (no net)
- J1 pad 4: Net-(J1-Pad4) -> (no net)
- J1 pad 6: Net-(J1-Pad6) -> Earth
- MCU1 pad 1: Net-(MCU1-Pad1) -> (no net)
- MCU1 pad 10: Net-(MCU1-Pad10) -> (no net)
- MCU1 pad 100: Net-(MCU1-Pad100) -> (no net)
- MCU1 pad 11: Net-(MCU1-Pad11) -> (no net)
- MCU1 pad 12: Net-(MCU1-Pad12) -> (no net)
- MCU1 pad 13: Net-(MCU1-Pad13) -> (no net)
- MCU1 pad 14: Net-(MCU1-Pad14) -> (no net)
- MCU1 pad 15: Net-(MCU1-Pad15) -> (no net)
- MCU1 pad 16: Net-(MCU1-Pad16) -> (no net)
- MCU1 pad 17: Net-(MCU1-Pad17) -> (no net)
- MCU1 pad 18: Net-(MCU1-Pad18) -> (no net)
- MCU1 pad 19: Net-(MCU1-Pad19) -> (no net)
- MCU1 pad 2: Net-(MCU1-Pad2) -> (no net)
- MCU1 pad 20: Net-(MCU1-Pad20) -> (no net)
- MCU1 pad 21: Net-(MCU1-Pad21) -> (no net)
- MCU1 pad 22: Net-(MCU1-Pad22) -> (no net)
- MCU1 pad 23: Net-(MCU1-Pad23) -> (no net)
- MCU1 pad 24: Net-(MCU1-Pad24) -> (no net)
- MCU1 pad 25: Net-(MCU1-Pad25) -> (no net)
- MCU1 pad 26: Net-(MCU1-Pad26) -> (no net)
- MCU1 pad 27: Net-(MCU1-Pad27) -> (no net)
- MCU1 pad 28: Net-(MCU1-Pad28) -> (no net)
- MCU1 pad 29: Net-(MCU1-Pad29) -> (no net)
- MCU1 pad 3: Net-(MCU1-Pad3) -> (no net)
- MCU1 pad 30: Net-(MCU1-Pad30) -> (no net)
- MCU1 pad 31: Net-(MCU1-Pad31) -> (no net)
- MCU1 pad 32: Net-(MCU1-Pad32) -> (no net)
- MCU1 pad 33: Net-(MCU1-Pad33) -> (no net)
- MCU1 pad 34: Net-(MCU1-Pad34) -> (no net)
- MCU1 pad 35: Net-(MCU1-Pad35) -> (no net)
- MCU1 pad 36: Net-(MCU1-Pad36) -> (no net)
- MCU1 pad 37: Net-(MCU1-Pad37) -> (no net)
- MCU1 pad 38: Net-(MCU1-Pad38) -> (no net)
- MCU1 pad 39: Net-(MCU1-Pad39) -> (no net)
- MCU1 pad 4: Net-(MCU1-Pad4) -> (no net)
- MCU1 pad 40: Net-(MCU1-Pad40) -> (no net)
- MCU1 pad 41: Net-(MCU1-Pad41) -> (no net)
- MCU1 pad 42: Net-(MCU1-Pad42) -> (no net)
- MCU1 pad 43: Net-(MCU1-Pad43) -> (no net)
- MCU1 pad 44: Net-(MCU1-Pad44) -> (no net)
- MCU1 pad 45: Net-(MCU1-Pad45) -> (no net)
- MCU1 pad 46: Net-(MCU1-Pad46) -> (no net)
- MCU1 pad 47: Net-(MCU1-Pad47) -> (no net)
- MCU1 pad 48: Net-(MCU1-Pad48) -> (no net)
- MCU1 pad 49: Net-(MCU1-Pad49) -> (no net)
- MCU1 pad 5: Net-(MCU1-Pad5) -> (no net)
- MCU1 pad 50: Net-(MCU1-Pad50) -> (no net)
- MCU1 pad 51: Net-(MCU1-Pad51) -> (no net)
- MCU1 pad 52: Net-(MCU1-Pad52) -> (no net)
- MCU1 pad 53: Net-(MCU1-Pad53) -> (no net)
- MCU1 pad 54: Net-(MCU1-Pad54) -> (no net)
- MCU1 pad 55: Net-(MCU1-Pad55) -> (no net)
- MCU1 pad 56: Net-(MCU1-Pad56) -> (no net)
- MCU1 pad 57: Net-(MCU1-Pad57) -> (no net)
- MCU1 pad 58: Net-(MCU1-Pad58) -> (no net)
- MCU1 pad 59: Net-(MCU1-Pad59) -> (no net)
- MCU1 pad 6: Net-(MCU1-Pad6) -> (no net)
- MCU1 pad 60: Net-(MCU1-Pad60) -> (no net)
- MCU1 pad 61: Net-(MCU1-Pad61) -> (no net)
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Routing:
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- added copper zone on F.Cu, net Earth
- added copper zone on F.Cu, net GND
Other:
- outline, holes or cut-outs redrawn
- rule pad_to_mask_clearance: 0 -> 0.05
- rule trace_min: 0.2 -> 0.15
- rule via_min_size: 0.4 -> 0.6

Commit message: added vias
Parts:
- moved D1034 144.6 mm to (363.5, 28.2)
- moved DCDC1 144.6 mm to (336.4, 55.5)
- moved R129 144.6 mm to (340.7, 54.1)
- moved R131 144.6 mm to (362.7, 34.5)
- moved U2 144.6 mm to (376.4, 26.8)
- moved C1 144.6 mm to (326.2, 35.8)
- moved C10 144.6 mm to (367.1, 26.9)
- moved C2 144.6 mm to (330.7, 35.8)
- moved C3 144.6 mm to (326.2, 62.8)
- moved C4 144.6 mm to (339.3, 58.8)
- moved C7 144.6 mm to (330.7, 62.8)
- moved C8 144.6 mm to (363.2, 31.8)
- moved D1035 144.6 mm to (358.1, 31.7)
- moved L1 144.6 mm to (337.5, 46.2)
- moved MCU1 144.6 mm to (380.2, 58.1)
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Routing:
- net GND: vias 0 -> 131
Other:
- board size 150 x 150 mm -> 200 x 180 mm

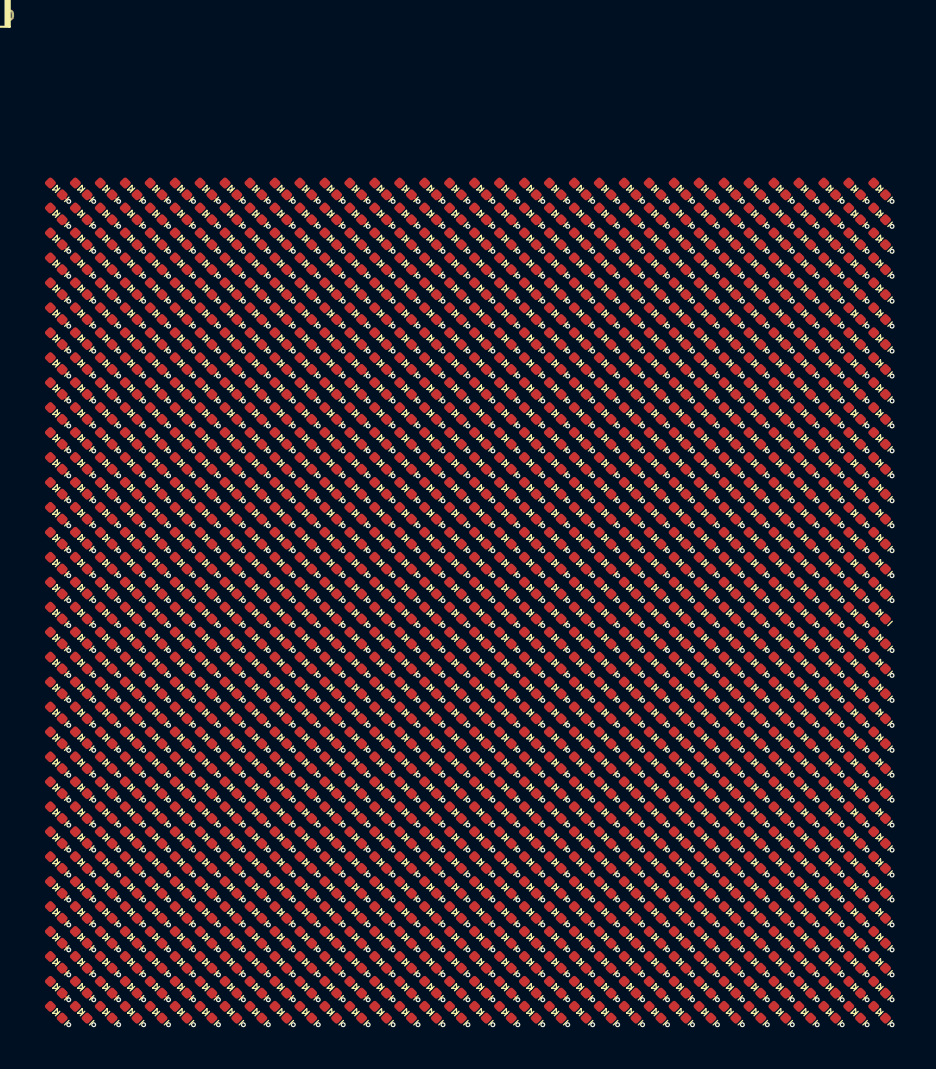
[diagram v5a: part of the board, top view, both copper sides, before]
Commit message: led matrix schematic page completed
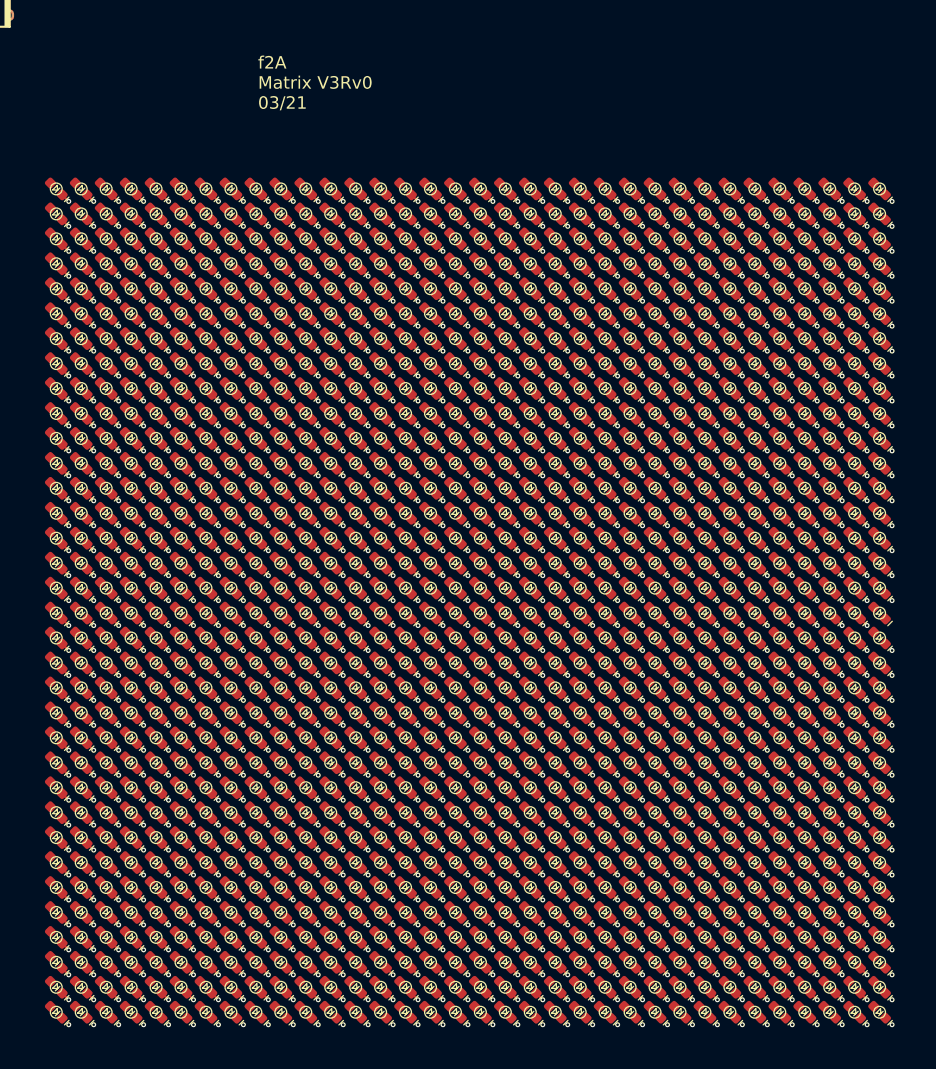
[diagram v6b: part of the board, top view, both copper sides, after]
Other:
- board text added: "f2A Matrix V3Rv0 03/21"
